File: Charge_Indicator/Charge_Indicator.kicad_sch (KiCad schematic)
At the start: 50 parts, among them J1 1984617

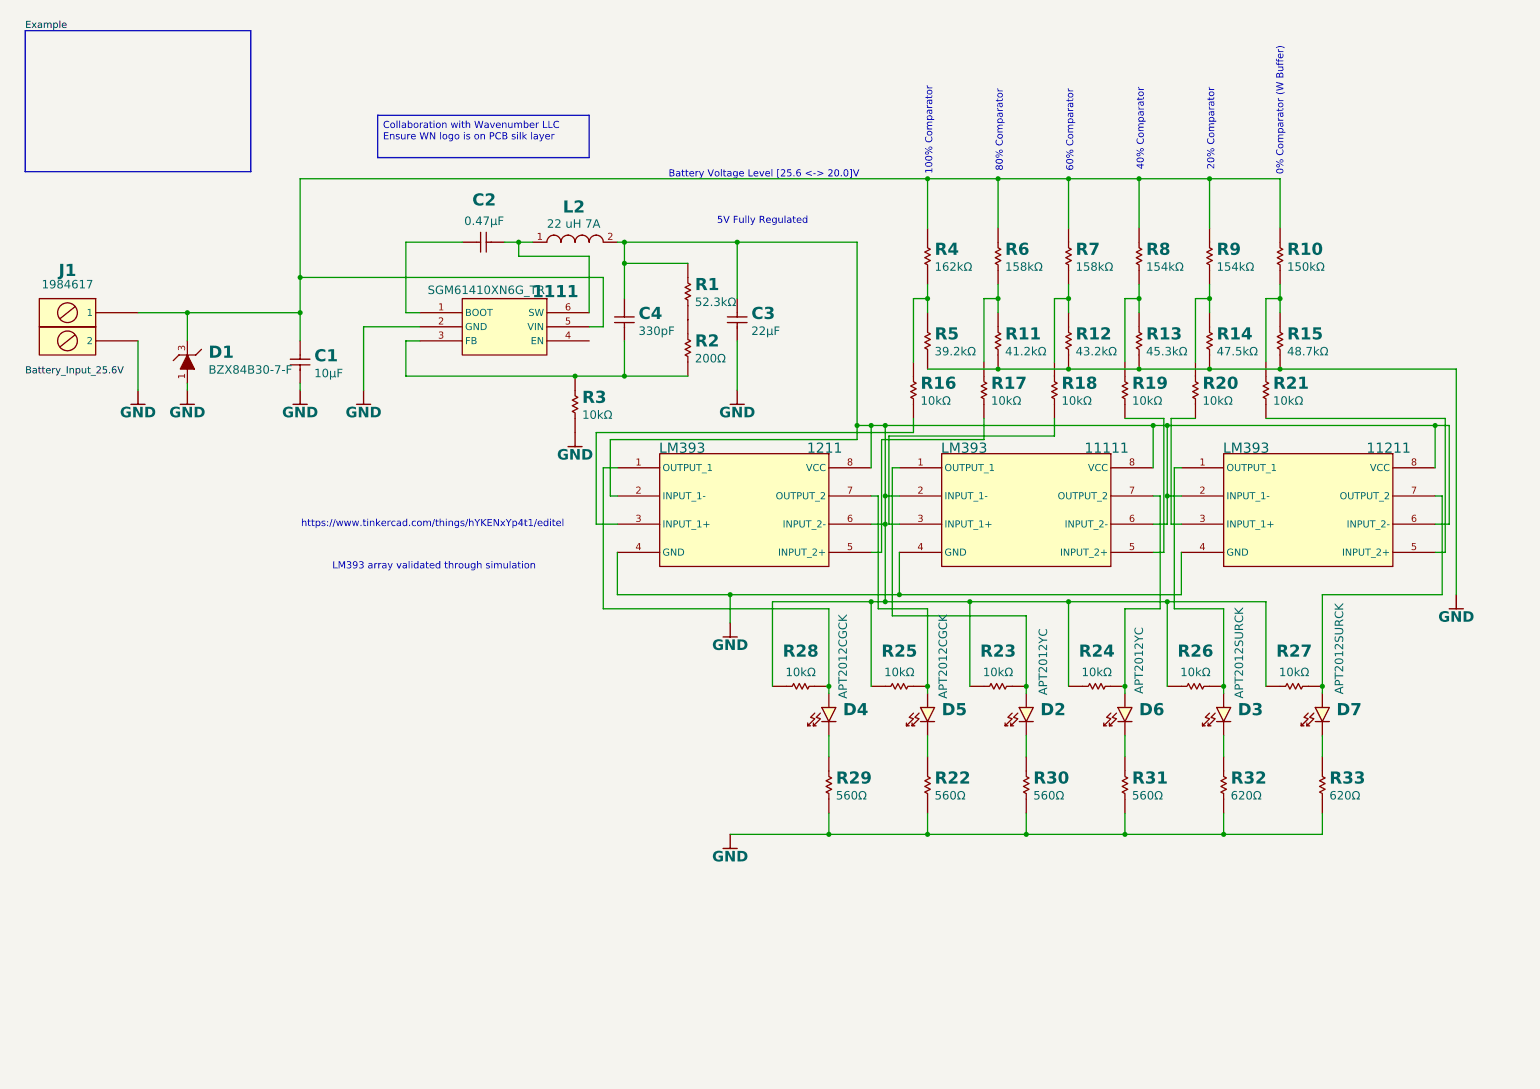
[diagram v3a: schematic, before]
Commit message: Using TI chips for power detection putting everything together.
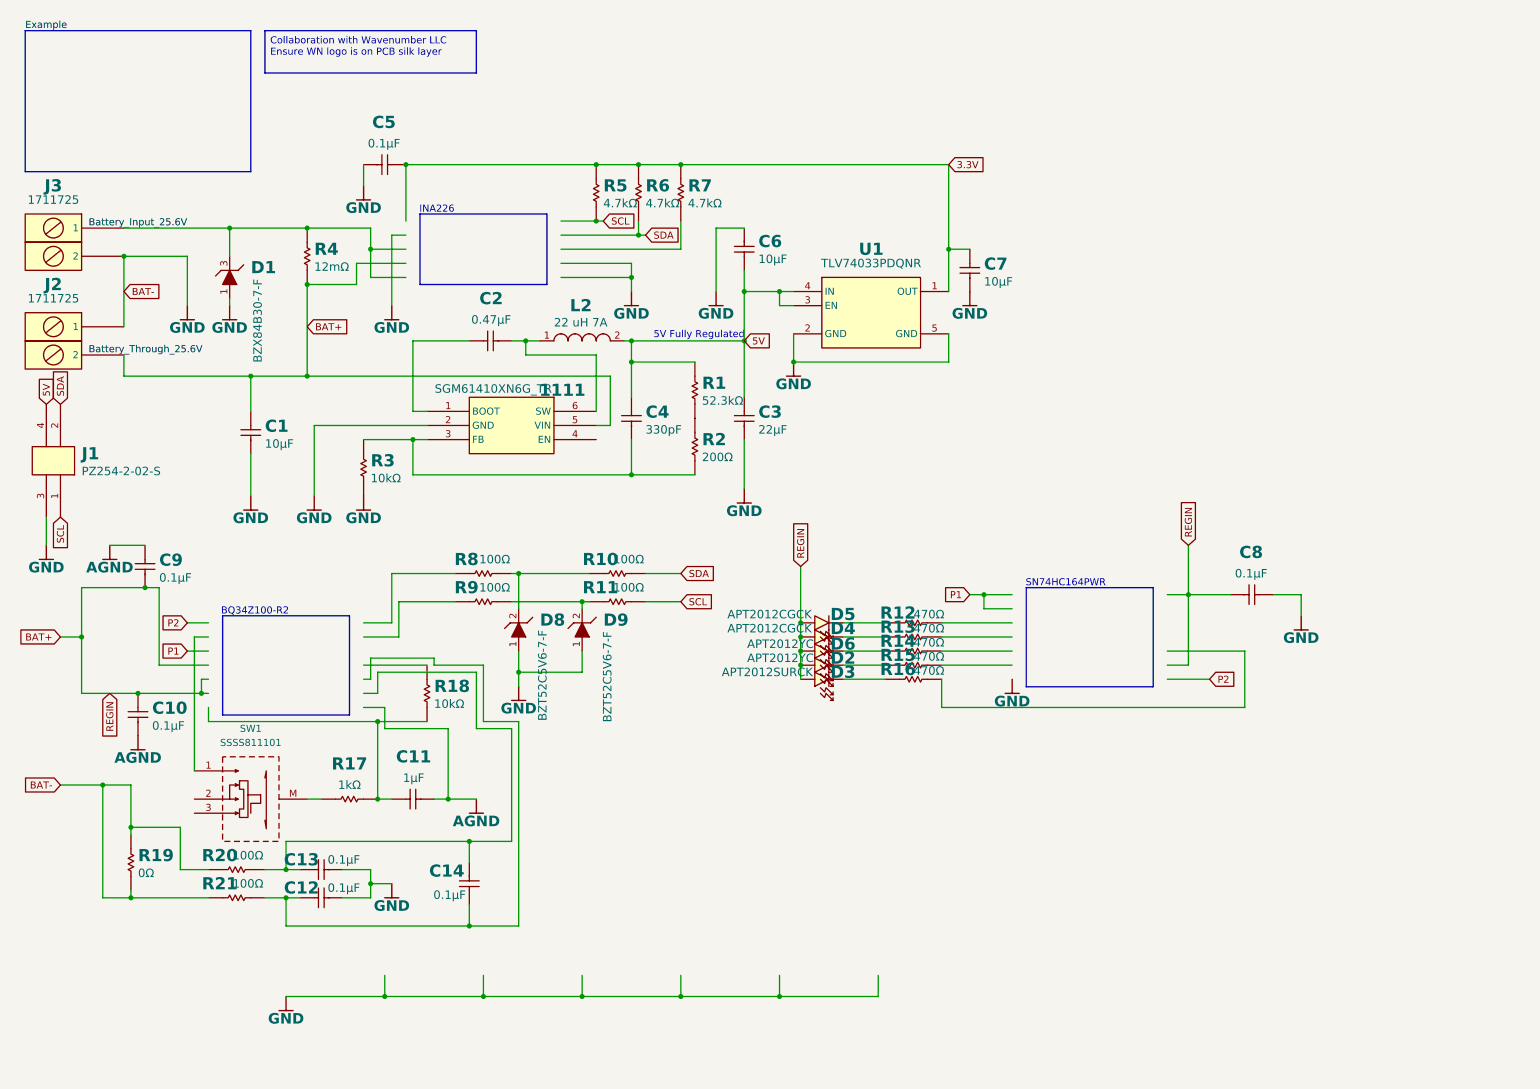
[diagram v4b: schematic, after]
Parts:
- removed 11111, 11211, 1211: LM393, wavenumber:LM393, symbol wn__wavenumber:LM393
- removed D7: APT2012SURCK, wavenumber:LED-0805-RED, symbol wn__wavenumber:LED-RED
- removed J1: 1984617, wavenumber:1984617, symbol wn__wavenumber:1984617
- removed R22, R29, R30, R31: 560Ω, wavenumber:R0603_0.55MM_HD, symbol wn__wavenumber:R_2P
- removed R23, R24, R25, R26, R27, R28: 10kΩ, wavenumber:R0603_0.55MM_HD, symbol wn__wavenumber:R_2P
- removed R32, R33: 620Ω, wavenumber:R0603_0.55MM_HD, symbol wn__wavenumber:R_2P
- added C10, C12, C13, C14, C5, C8, C9: 0.1µF, wavenumber:C0603_0.90MM_MD, symbol wn__wavenumber:C_2P_NP
- added C11: 1µF, wavenumber:C0603_0.90MM_MD, symbol wn__wavenumber:C_2P_NP
- added C6, C7: 10µF, wavenumber:C1206_1.80MM_MD, symbol wn__wavenumber:C_2P_NP
- added D8, D9: BZT52C5V6-7-F, wavenumber:D_SOD-123_P, symbol wn__wavenumber:DZ_1A_2C
- added J1: PZ254-2-02-S, wavenumber:PZ254-2-02-S, symbol wn__wavenumber:CON-2-2
- added J2, J3: 1711725, wavenumber:1711725, symbol wn__wavenumber:1711725
- added SW1: SSSS811101, wavenumber:SSSS811101, symbol wn__wavenumber:SSSS811101
- added U1: TLV74033PDQNR, symbol wavenumber:TLV74033PDQNR
- R10: value 150kΩ -> 100Ω; Manufacturer Part Number ERJ-3EKF1503V -> ERJ-3EKF1000V; cad-reference ERJ-3EKF1503V -> ERJ-3EKF1000V
- R11: value 41.2kΩ -> 100Ω; Manufacturer Part Number ERJ-3EKF4122V -> ERJ-3EKF1000V; cad-reference ERJ-3EKF4122V -> ERJ-3EKF1000V
- R12: value 43.2kΩ -> 470Ω; Manufacturer Part Number ERJ-3EKF4322V -> ERJ-3EKF4700V; cad-reference ERJ-3EKF4322V -> ERJ-3EKF4700V
- R13: value 45.3kΩ -> 470Ω; Manufacturer Part Number ERJ-3EKF4532V -> ERJ-3EKF4700V; cad-reference ERJ-3EKF4532V -> ERJ-3EKF4700V
- R14: value 47.5kΩ -> 470Ω; Manufacturer Part Number ERJ-3EKF4752V -> ERJ-3EKF4700V; cad-reference ERJ-3EKF4752V -> ERJ-3EKF4700V
- R15: value 48.7kΩ -> 470Ω; Manufacturer Part Number ERJ-3EKF4872V -> ERJ-3EKF4700V; cad-reference ERJ-3EKF4872V -> ERJ-3EKF4700V
- R16: value 10kΩ -> 470Ω; Manufacturer Part Number ERJ-3EKF1002V -> ERJ-3EKF4700V; cad-reference ERJ-3EKF1002V -> ERJ-3EKF4700V
- R17: value 10kΩ -> 1kΩ; Manufacturer Part Number ERJ-3EKF1002V -> ERJ-3EKF1001V; cad-reference ERJ-3EKF1002V -> ERJ-3EKF1001V
- R18: footprint wavenumber:R0603_0.55MM_HD -> wavenumber:R1206_0.70MM_HD; Manufacturer Part Number ERJ-3EKF1002V -> ERJ-8ENF1002V; cad-reference ERJ-3EKF1002V -> ERJ-8ENF1002V
- R19: value 10kΩ -> 0Ω; footprint wavenumber:R0603_0.55MM_HD -> wavenumber:R0201_0.26MM_HD; Manufacturer Part Number ERJ-3EKF1002V -> ERJ-1GE0R00C; cad-reference ERJ-3EKF1002V -> ERJ-1GE0R00C
- R20, R21: value 10kΩ -> 100Ω; Manufacturer Part Number ERJ-3EKF1002V -> ERJ-3EKF1000V; cad-reference ERJ-3EKF1002V -> ERJ-3EKF1000V
- R4: value 162kΩ -> 12mΩ; footprint wavenumber:R0603_0.55MM_HD -> wavenumber:R1206_0.65MM_MD; Manufacturer Panasonic Electronic Components -> YAGEO; Manufacturer Part Number ERJ-3EKF1623V -> RL1206FR-070R012L; cad-reference ERJ-3EKF1623V -> RL1206FR-070R012L
- R5: value 39.2kΩ -> 4.7kΩ; Manufacturer Part Number ERJ-3EKF3922V -> ERJ-3EKF4701V; cad-reference ERJ-3EKF3922V -> ERJ-3EKF4701V
- R6, R7: value 158kΩ -> 4.7kΩ; Manufacturer Part Number ERJ-3EKF1583V -> ERJ-3EKF4701V; cad-reference ERJ-3EKF1583V -> ERJ-3EKF4701V
- R8, R9: value 154kΩ -> 100Ω; Manufacturer Part Number ERJ-3EKF1543V -> ERJ-3EKF1000V; cad-reference ERJ-3EKF1543V -> ERJ-3EKF1000V
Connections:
- net GND: now also R19.1, R19.2, R20.1, R21.1, C12.2 (1), C13.2 (1), C5.2 (1), C6.2 (1), C7.2 (1), C8.1, D8.1 (A), D9.1 (A), J1.3, J2.1, J3.2, U1.2 (GND), U1.5 (GND); no longer R11.2, R12.2, R13.2, R14.2, R15.2, R5.2
- net BAT+: now reaches D5.A
- net BAT+: now also 1111.5 (VIN), C1.1, D2.A, D3.A, D4.A, D6.A, R4.2, C10.1, C8.2 (1), C9.2 (1), J2.2
- net at D5.C: now also R12.1
- net at D6.C: now also R14.1
- net at D4.C: now also R13.1
- net at D2.C: now also R15.1
- net 5V: now reaches C3.1, C4.1, L2.2, R1.1
- net 5V: now also C6.1, J1.4, U1.3 (EN), U1.4 (IN)
- net at R20.2: now also C13.1, C14.2 (1)
- net at R17.2: now also R18.1, C11.1
- net at R21.2: now also C12.1, C14.1
- net at D3.C: now also R16.1
- new net: R17.1, SW1.M
- new net: D1.3 (K), J3.1, R4.1
- new net: D9.2 (K), R11.1, R9.2
- new net: D8.2 (K), R10.1, R8.2
- new net 3.3V: C5.1, C7.1, R5.1, R6.1, R7.1, U1.1 (OUT)
- new net AGND: C10.2 (1), C11.2 (1), C9.1
- new net SCL: J1.1, R11.2, R5.2
- new net SDA: J1.2, R10.2, R6.2
- now unconnected: R7.2, R8.1, R9.1
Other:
- note added: "BQ34Z100-R2"
- note added: "INA226"
- note added: "SN74HC164PWR"
- note removed: "0% Comparator (W Buffer)"
- note removed: "100% Comparator"
- note removed: "20% Comparator"
- note removed: "40% Comparator"
- note removed: "60% Comparator"
- note removed: "80% Comparator"
- note removed: "Battery Voltage Level [25.6 <-> 20.0]V"
- note removed: "LM393 array validated through simulation"
- note removed: "https://www.tinkercad.com/things/hYKENxYp4t1/editel"
- moved on the sheet: 1111, C1, C2, C3, C4, D1, D3, D5, D6, L2, R1, R2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

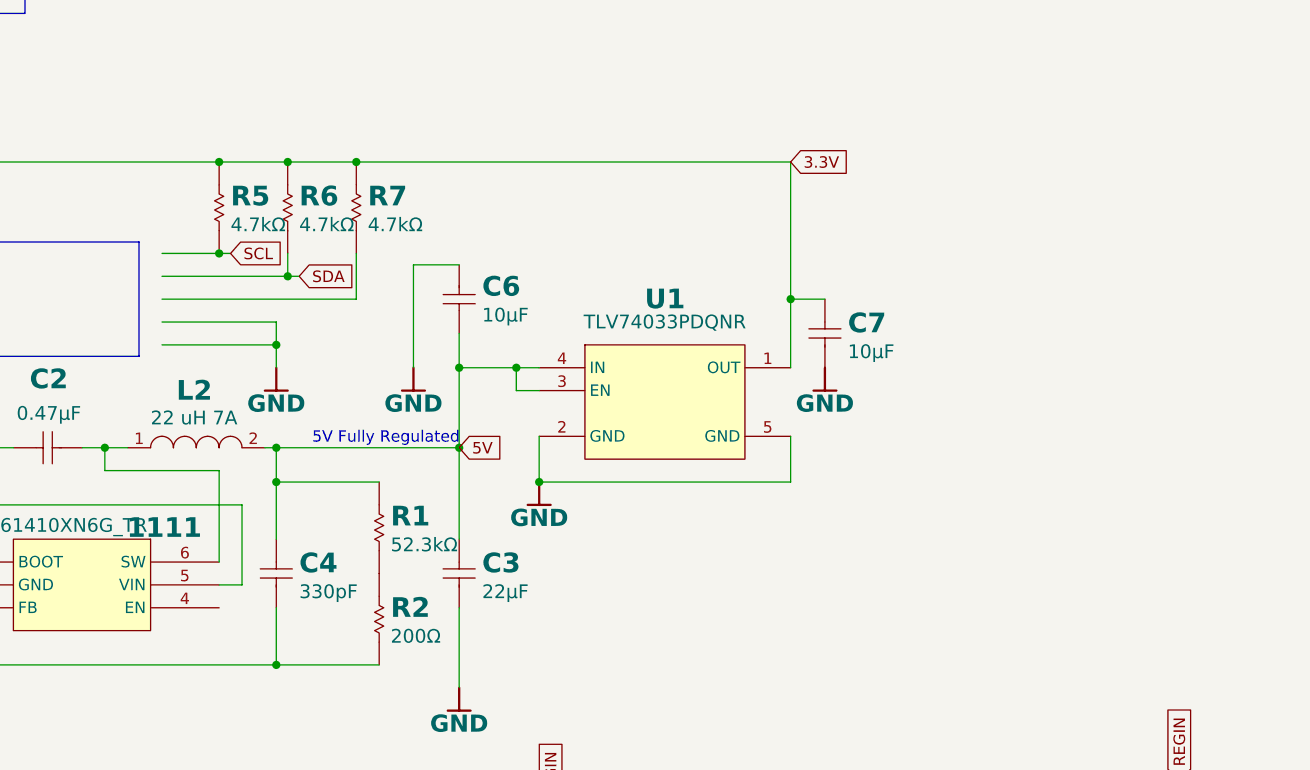
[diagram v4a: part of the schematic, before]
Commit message: Adding Zero Ohms and Test Points on 5 and 3.3 points
Summary of Changes:
- On the buck output is a test point and zero ohm to ensure there is 5V constant.
- On the regulator output is a test point and zero ohm to ensure there is 3.3V constant.
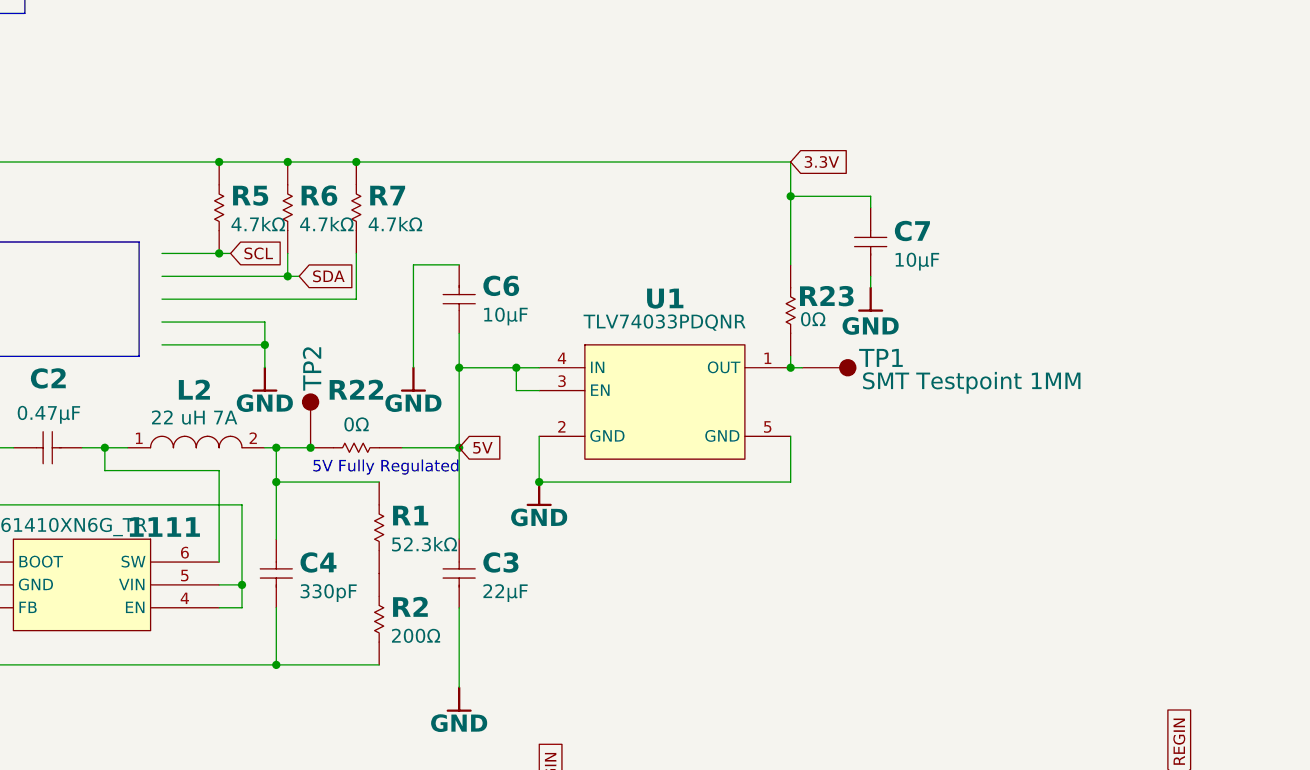
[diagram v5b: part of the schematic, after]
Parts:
- added R22, R23: 0Ω, wavenumber:R0201_0.26MM_HD, symbol wn__wavenumber:R_2P
- added TP1, TP2: SMT Testpoint 1MM, wavenumber:SMT_TP-1MM, symbol wn__wavenumber:SMT_TEST
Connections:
- net 3.3V: now also R23.2; no longer U1.1 (OUT)
- net 5V: now also R22.2; no longer C4.1, L2.2, R1.1
- net BAT+: now also 1111.4 (EN)
- new net: R23.1, TP1.1, U1.1 (OUT)
- new net: C4.1, L2.2, R1.1, R22.1, TP2.1
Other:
- moved on the sheet: C7
